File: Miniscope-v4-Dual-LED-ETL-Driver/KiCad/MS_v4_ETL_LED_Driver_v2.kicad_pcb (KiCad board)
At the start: 6 copper layers, 13.5 x 10.5 mm, 34 parts, among them J1 Conn_01x01, J10 Conn_01x05, J6 Conn_01x01, J7 Conn_01x01, U1 MAX14574EWL+, U2 TPL0102-100RUCR, U3 LTC3218, U4 LTC3218

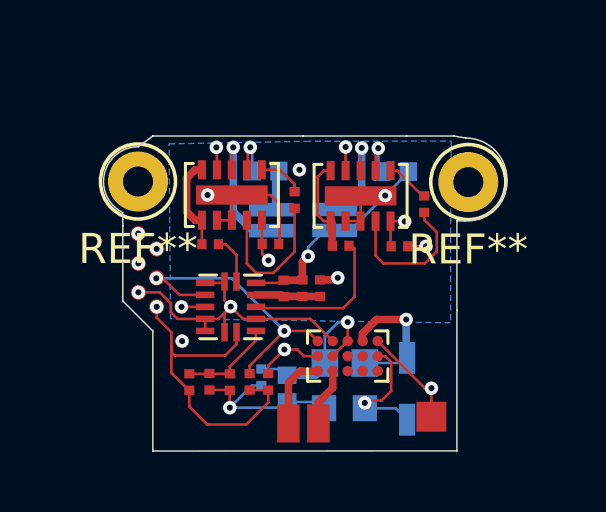
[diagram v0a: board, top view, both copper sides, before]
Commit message: Dual color rev2 ready for fab
Changes

- LEDs are now vertical instead of horizontal. This was changed to allow some tilt on the LEDs

- Thicker traces
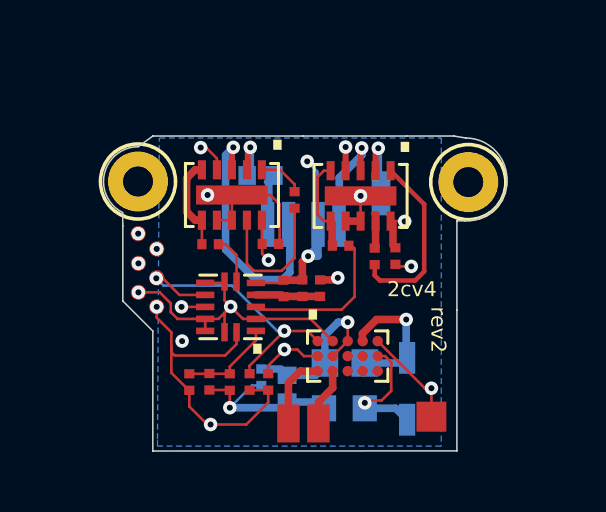
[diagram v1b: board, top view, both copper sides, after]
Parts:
- moved C9 2.40 mm to (20.7, 17.3), turned to 270 degrees
- moved C10 0.86 mm to (20.9, 15.2), turned to 270 degrees
- moved C8 0.35 mm to (21.4, 17.3), turned to 270 degrees
- moved D2 0.26 mm to (17.5, 16.2), turned to 180 degrees
- moved D3 0.26 mm to (19.1, 16.2), turned to 180 degrees
- moved C6 0.22 mm to (16.9, 14.6)
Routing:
- net Net-(C9-Pad2): track 1.46 -> 6.03 mm
- net Net-(D2-PadA): track 4.48 -> 8.59 mm
- net Net-(C9-Pad1): track 5.12 -> 1.10 mm
- net GND: track 40.0 -> 41.4 mm
- net +3V3: vias 5 -> 6
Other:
- board text added: "."
- board text added: "2cv4"
- board text added: "rev2"
- board text removed: "+"
- board text removed: "-"
